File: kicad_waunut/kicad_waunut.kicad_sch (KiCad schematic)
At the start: 76 parts, among them J1 Conn_01x06_Pin, J2 Conn_01x02_Pin, U1 ATtiny861A-S

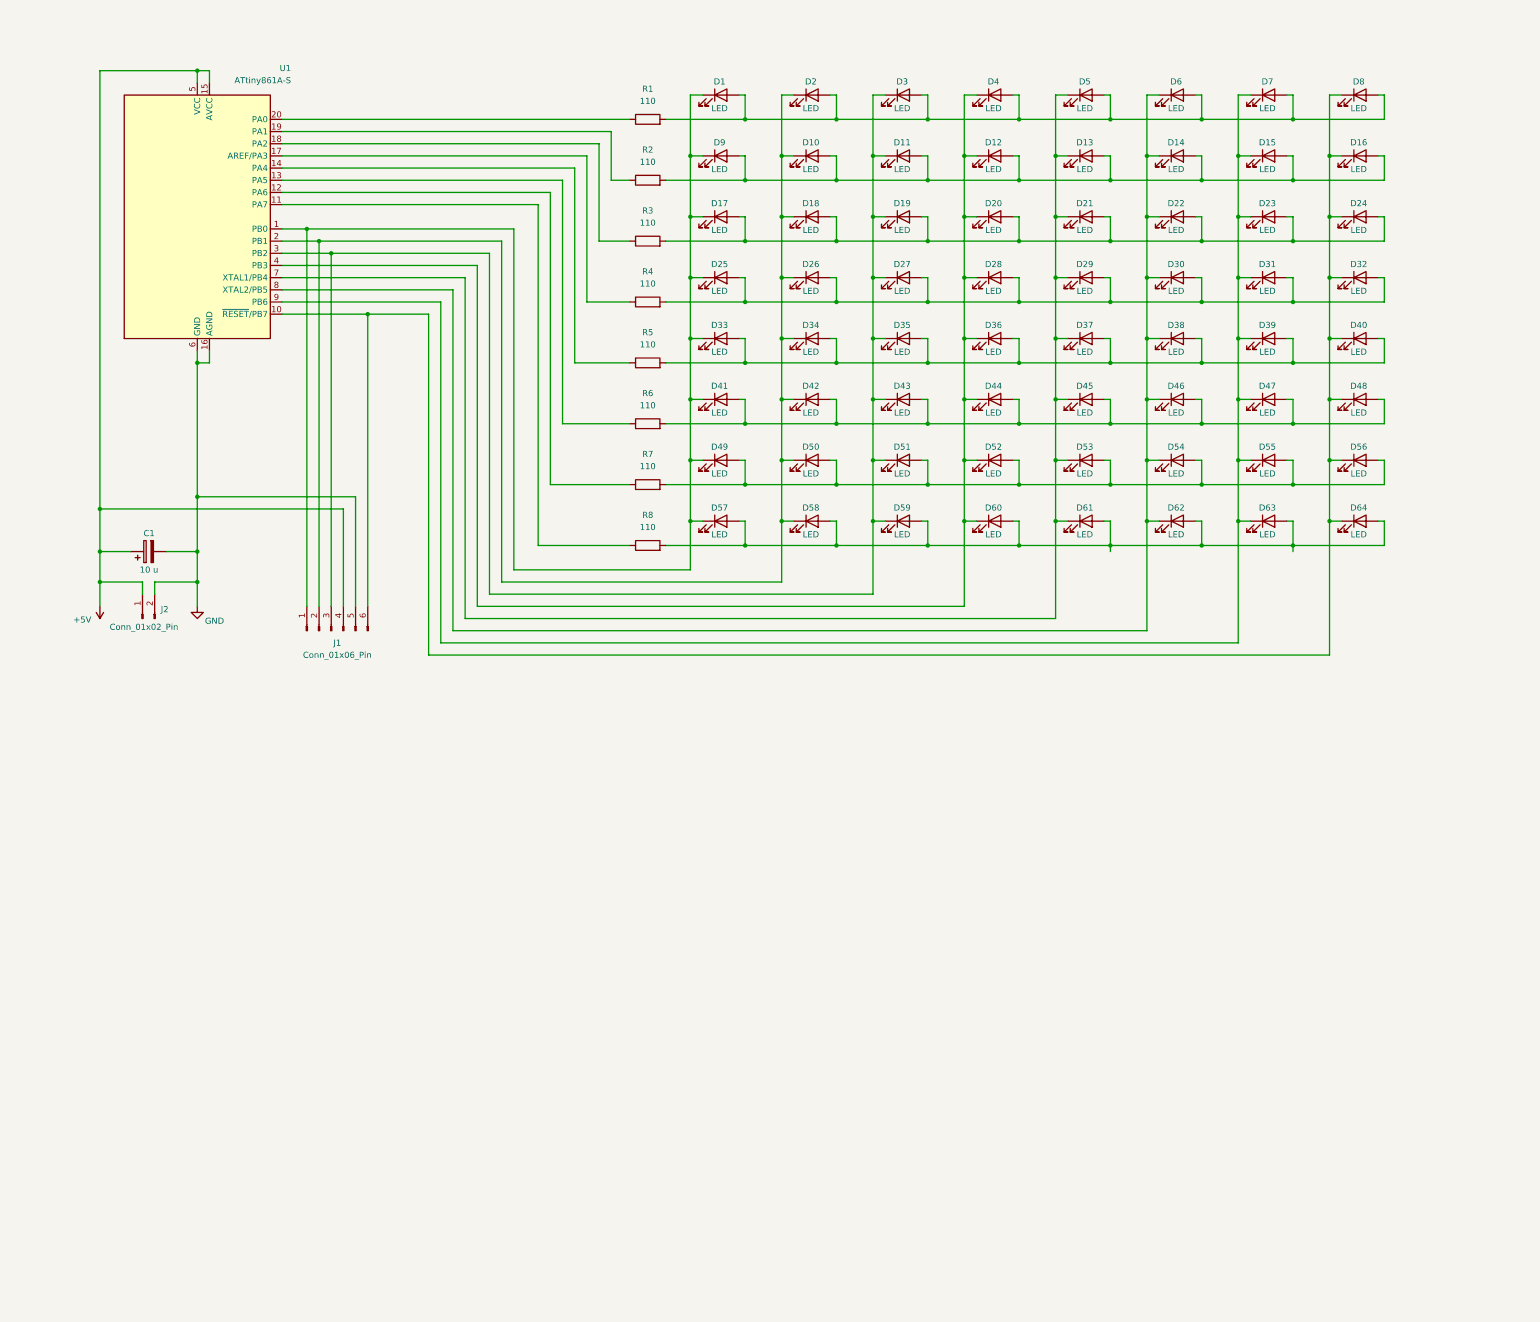
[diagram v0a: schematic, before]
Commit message: 2 lediä vilkkuu - vilkutus_2x.c
Jostain syystä kummallinen if statementti jossa 2 lediä palaa mutta eri
kirrkaudella.

Muutama ledi himmenee/kirkastuu. hmm...

Muuten jeba
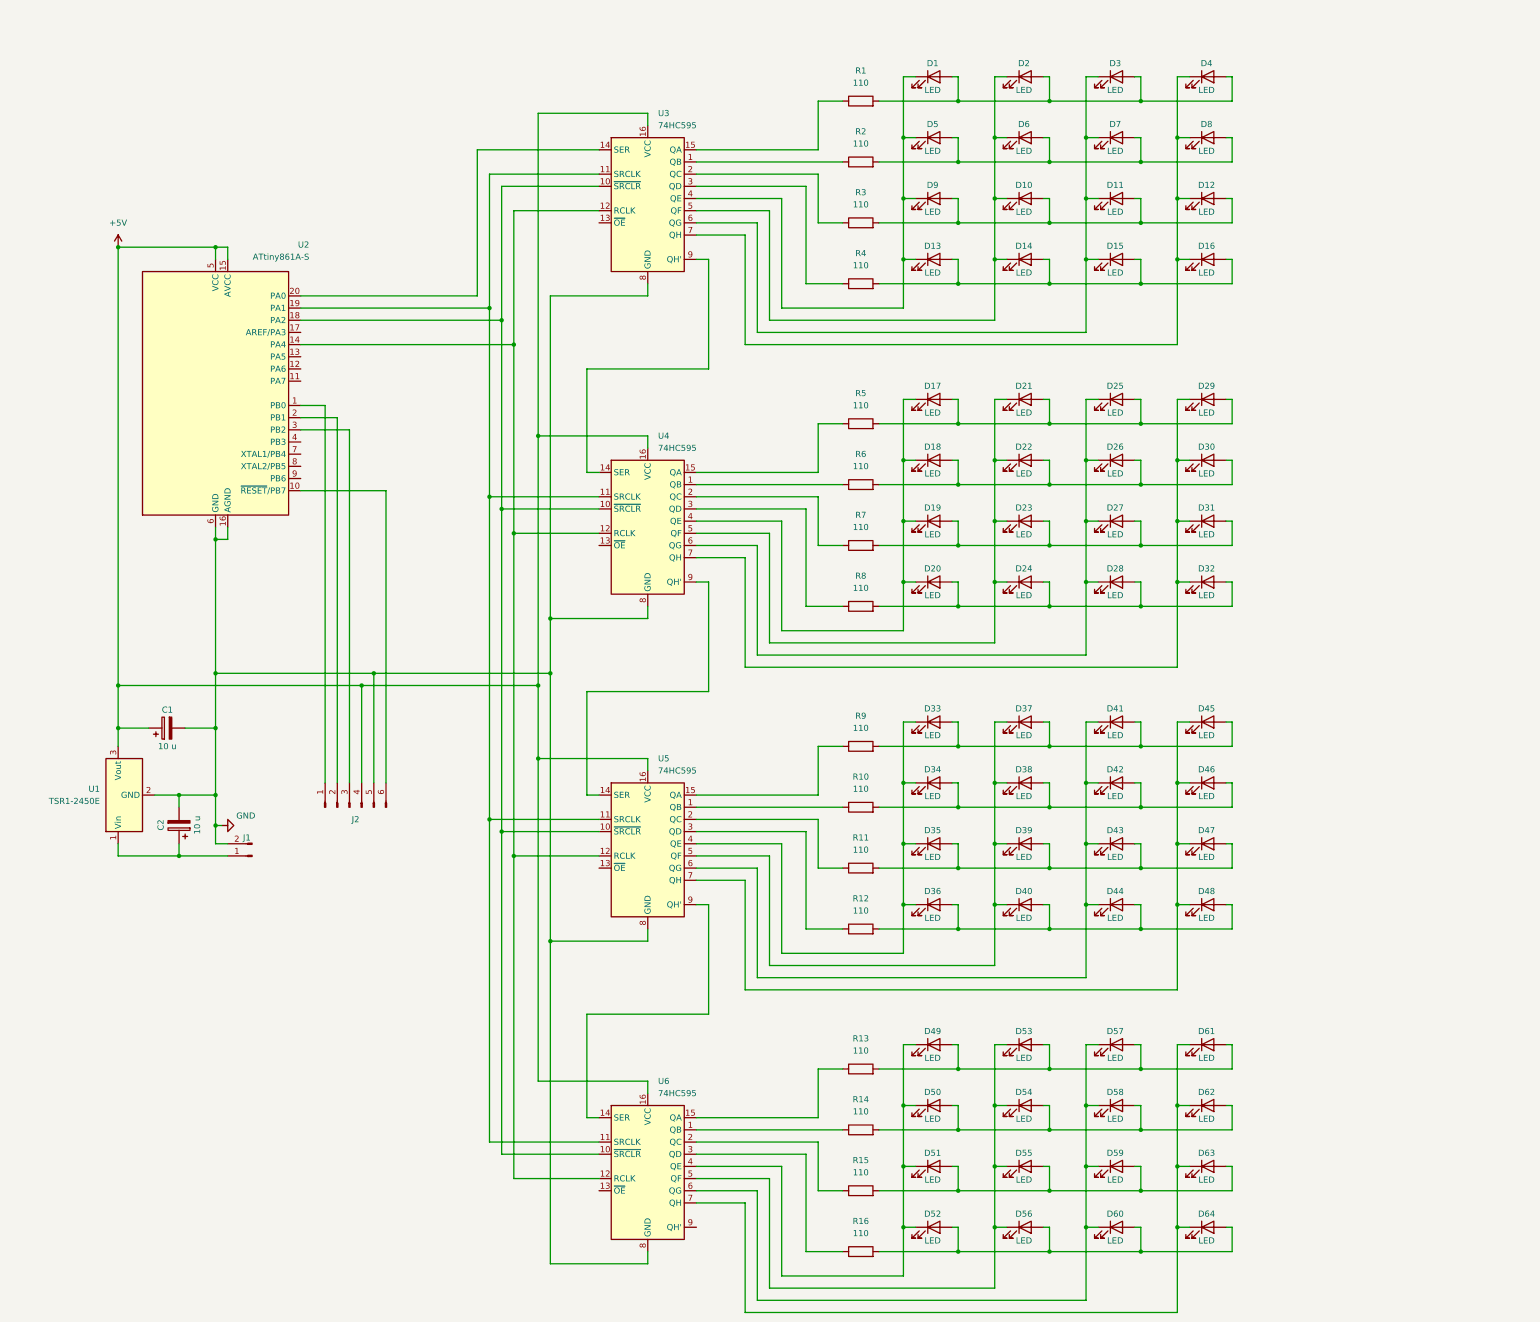
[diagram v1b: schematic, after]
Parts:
- added C2: 10 u, Capacitor_SMD:C_1210_3225Metric_Pad1.33x2.70mm_HandSolder, symbol Device:C_Polarized
- added R10, R11, R12, R13, R14, R15, R16, R9: 110, Resistor_SMD:R_1206_3216Metric_Pad1.30x1.75mm_HandSolder, symbol Device:R
- added U1: TSR1-2450E, Converter_DCDC:Converter_DCDC_TRACO_TSR-1_THT, symbol Regulator_Switching:TSR1-2450E
- added U3, U4, U5, U6: 74HC595, Package_SO:SOIC-16_3.9x9.9mm_P1.27mm, symbol 74xx:74HC595
- renumbered J2 to J1, J1 to J2, U1 to U2
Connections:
- net +5V: now also U1.3 (Vout), U3.16 (VCC), U4.16 (VCC), U5.16 (VCC), U6.16 (VCC); no longer J1.1 (Pin_1)
- net GND: now also C2.2, U1.2 (GND), U3.8 (GND), U4.8 (GND), U5.8 (GND), U6.8 (GND)
- net at D1.2 (A), D2.2 (A), D3.2 (A)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: no longer D5.2 (A), D6.2 (A), D7.2 (A), D8.2 (A)
- net at R4.1: now also U3.3 (QD); no longer U2.17 (AREF/PA3)
- net at R8.1: now also U4.3 (QD); no longer U2.11 (PA7)
- net at U2.18 (PA2): now also U3.10 (~{SRCLR}), U4.10 (~{SRCLR}), U5.10 (~{SRCLR}), U6.10 (~{SRCLR}); no longer R3.1
- net at U2.14 (PA4): now also U3.12 (RCLK), U4.12 (RCLK), U5.12 (RCLK), U6.12 (RCLK); no longer R5.1
- net at U2.20 (PA0): now also U3.14 (SER); no longer R1.1
- net at R6.1: now also U4.1 (QB); no longer U2.13 (PA5)
- net at R7.1: now also U4.2 (QC); no longer U2.12 (PA6)
- net at U2.19 (PA1): now also U3.11 (SRCLK), U4.11 (SRCLK), U5.11 (SRCLK), U6.11 (SRCLK); no longer R2.1
- new net: D45.1 (K), D46.1 (K), D47.1 (K), D48.1 (K), U5.7 (QH)
- new net: D36.2 (A), D40.2 (A), D44.2 (A), D48.2 (A), R12.2
- new net: D17.1 (K), D18.1 (K), D19.1 (K), D20.1 (K), U4.4 (QE)
- new net: D19.2 (A), D23.2 (A), D27.2 (A), D31.2 (A), R7.2
- new net: D21.1 (K), D22.1 (K), D23.1 (K), D24.1 (K), U4.5 (QF)
- new net: D17.2 (A), D21.2 (A), D25.2 (A), D29.2 (A), R5.2
- new net: D34.2 (A), D38.2 (A), D42.2 (A), D46.2 (A), R10.2
- new net: D20.2 (A), D24.2 (A), D28.2 (A), D32.2 (A), R8.2
- new net: D37.1 (K), D38.1 (K), D39.1 (K), D40.1 (K), U5.5 (QF)
- new net: D12.1 (K), D16.1 (K), D4.1 (K), D8.1 (K), U3.7 (QH)
- new net: D5.2 (A), D6.2 (A), D7.2 (A), D8.2 (A), R2.2
- new net: D41.1 (K), D42.1 (K), D43.1 (K), D44.1 (K), U5.6 (QG)
- new net: D53.1 (K), D54.1 (K), D55.1 (K), D56.1 (K), U6.5 (QF)
- new net: D52.2 (A), D56.2 (A), D60.2 (A), D64.2 (A), R16.2
- new net: D57.1 (K), D58.1 (K), D59.1 (K), D60.1 (K), U6.6 (QG)
- new net: D50.2 (A), D54.2 (A), D58.2 (A), D62.2 (A), R14.2
- new net: D29.1 (K), D30.1 (K), D31.1 (K), D32.1 (K), U4.7 (QH)
- new net: D35.2 (A), D39.2 (A), D43.2 (A), D47.2 (A), R11.2
- new net: D49.1 (K), D50.1 (K), D51.1 (K), D52.1 (K), U6.4 (QE)
- new net: D33.2 (A), D37.2 (A), D41.2 (A), D45.2 (A), R9.2
- new net: D51.2 (A), D55.2 (A), D59.2 (A), D63.2 (A), R15.2
- new net: R14.1, U6.1 (QB)
- new net: U5.9 (QH'), U6.14 (SER)
- new net: R13.1, U6.15 (QA)
- new net: R15.1, U6.2 (QC)
- new net: R16.1, U6.3 (QD)
- new net: D61.1 (K), D62.1 (K), D63.1 (K), D64.1 (K), U6.7 (QH)
- new net: R12.1, U5.3 (QD)
- new net: D13.2 (A), D14.2 (A), D15.2 (A), D16.2 (A), R4.2
- new net: C2.1, J1.1 (Pin_1), U1.1 (Vin)
- new net: D33.1 (K), D34.1 (K), D35.1 (K), D36.1 (K), U5.4 (QE)
- new net: D11.1 (K), D15.1 (K), D3.1 (K), D7.1 (K), U3.6 (QG)
- new net: D1.1 (K), D13.1 (K), D5.1 (K), D9.1 (K), U3.4 (QE)
- new net: D10.2 (A), D11.2 (A), D12.2 (A), D9.2 (A), R3.2
- new net: D25.1 (K), D26.1 (K), D27.1 (K), D28.1 (K), U4.6 (QG)
- new net: R3.1, U3.2 (QC)
- new net: R2.1, U3.1 (QB)
- new net: R1.1, U3.15 (QA)
- new net: D10.1 (K), D14.1 (K), D2.1 (K), D6.1 (K), U3.5 (QF)
- new net: U3.9 (QH'), U4.14 (SER)
- new net: D49.2 (A), D53.2 (A), D57.2 (A), D61.2 (A), R13.2
- new net: J2.1 (Pin_1), U2.1 (PB0)
- new net: J2.2 (Pin_2), U2.2 (PB1)
- new net: J2.3 (Pin_3), U2.3 (PB2)
- new net: J2.6 (Pin_6), U2.10 (~{RESET}/PB7)
- new net: D18.2 (A), D22.2 (A), D26.2 (A), D30.2 (A), R6.2
- new net: R5.1, U4.15 (QA)
- new net: U4.9 (QH'), U5.14 (SER)
- new net: R10.1, U5.1 (QB)
- new net: R9.1, U5.15 (QA)
- new net: R11.1, U5.2 (QC)
- now unconnected: U2.4 (PB3), U2.7 (XTAL1/PB4), U2.8 (XTAL2/PB5), U2.9 (PB6)
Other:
- moved on the sheet: C1, D1, J1, J2, R1, R2, R3, R4, U2

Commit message: Waunujen skemaa muutettu. README tiedostoja päivitetty.
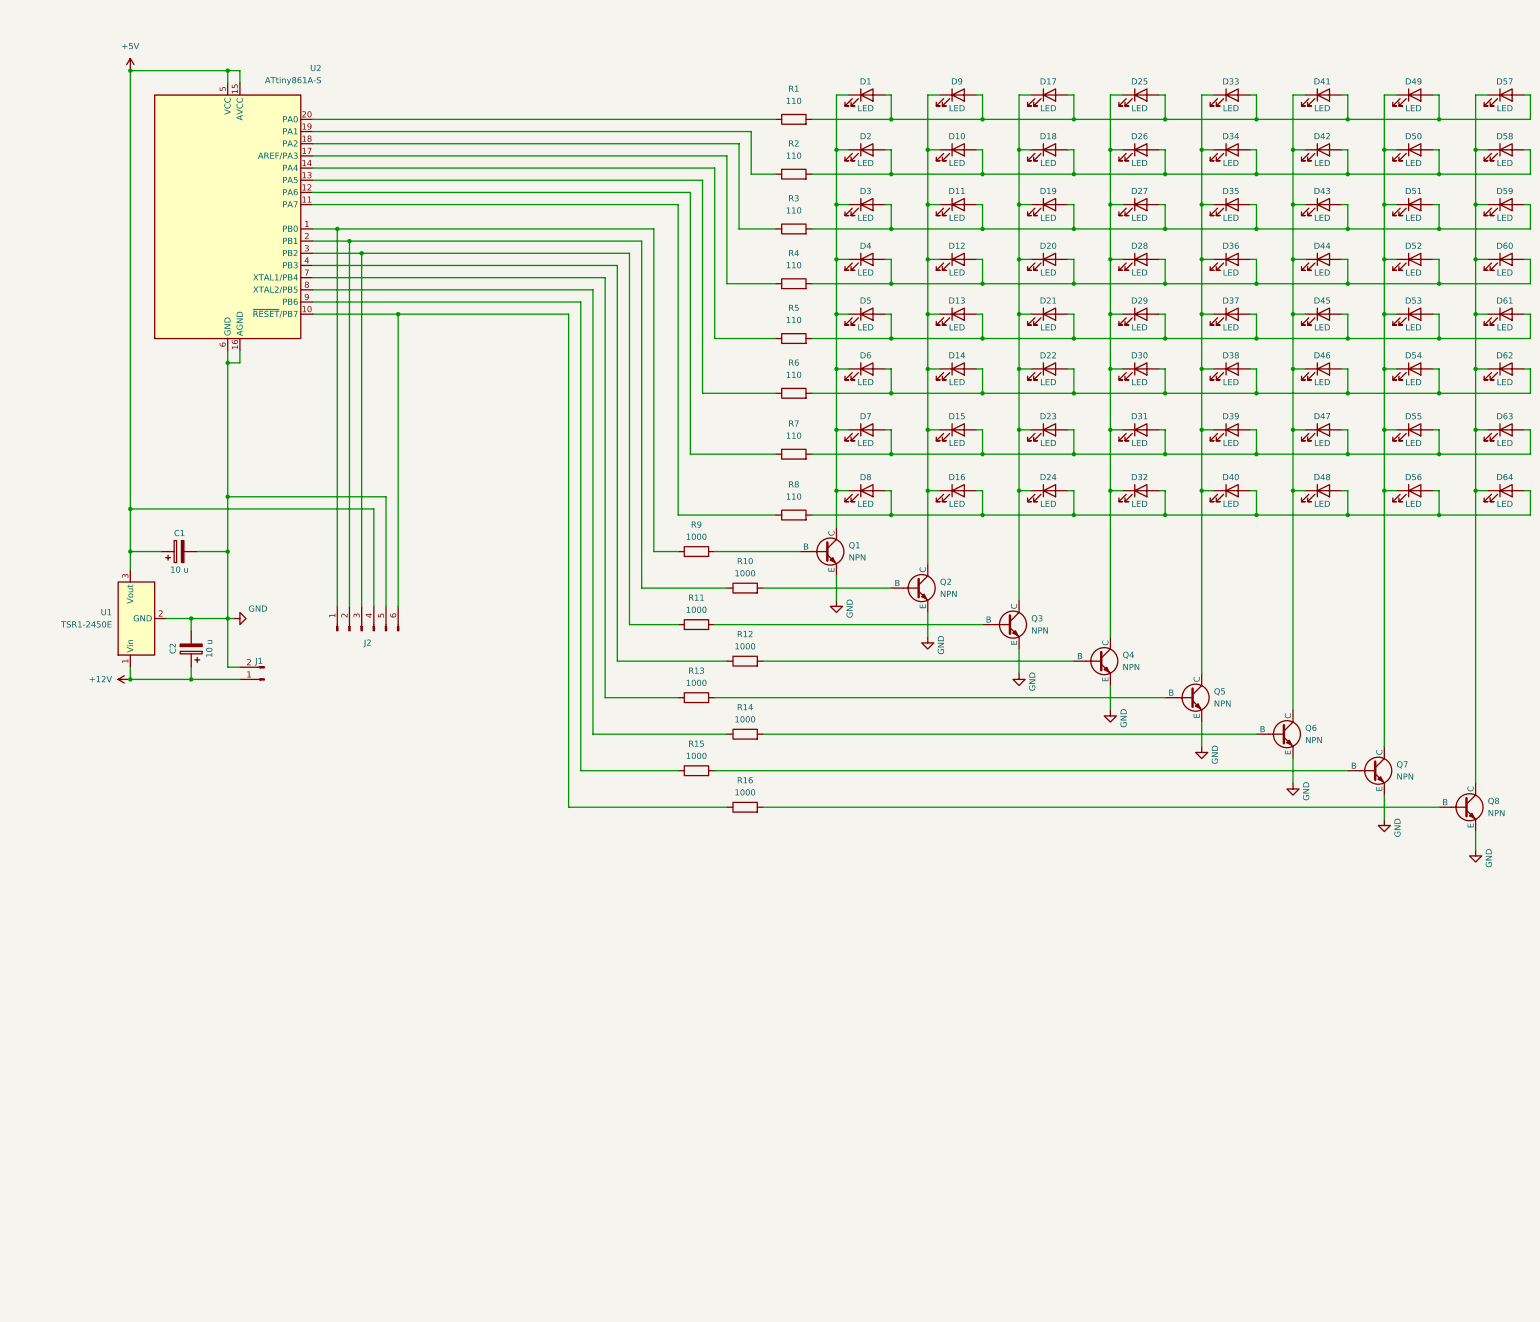
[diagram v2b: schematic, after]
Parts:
- removed U3, U4, U5, U6: 74HC595, Package_SO:SOIC-16_3.9x9.9mm_P1.27mm, symbol 74xx:74HC595
- added Q1, Q2, Q3, Q4, Q5, Q6, Q7, Q8: NPN, Package_TO_SOT_SMD:SOT-23, symbol Simulation_SPICE:NPN
- R10, R11, R12, R13, R14, R15, R16, R9: value 110 -> 1000
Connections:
- net GND: now also Q1.3 (E), Q2.3 (E), Q3.3 (E), Q4.3 (E), Q5.3 (E), Q6.3 (E), Q7.3 (E), Q8.3 (E)
- net at D45.1 (K), D46.1 (K), D47.1 (K)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: now also D41.1 (K), D42.1 (K), D43.1 (K), D44.1 (K), Q6.1 (C)
- net at D17.1 (K), D18.1 (K), D19.1 (K)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: now also D21.1 (K), D22.1 (K), D23.1 (K), D24.1 (K), Q3.1 (C)
- net at D23.2 (A), D31.2 (A), R7.2: now also D15.2 (A), D39.2 (A), D47.2 (A), D55.2 (A), D63.2 (A), D7.2 (A); no longer D19.2 (A), D27.2 (A)
- net at D21.2 (A), D29.2 (A), R5.2: now also D13.2 (A), D37.2 (A), D45.2 (A), D5.2 (A), D53.2 (A), D61.2 (A); no longer D17.2 (A), D25.2 (A)
- net at D24.2 (A), D32.2 (A), R8.2: now also D16.2 (A), D40.2 (A), D48.2 (A), D56.2 (A), D64.2 (A), D8.2 (A); no longer D20.2 (A), D28.2 (A)
- net at D37.1 (K), D38.1 (K), D39.1 (K)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: now also D33.1 (K), D34.1 (K), D35.1 (K), D36.1 (K), Q5.1 (C)
- net at D4.1 (K), D8.1 (K): now also D1.1 (K), D2.1 (K), D3.1 (K), D5.1 (K), D6.1 (K), D7.1 (K), Q1.1 (C); no longer D12.1 (K), D16.1 (K)
- net at D53.1 (K), D54.1 (K), D55.1 (K)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: now also D49.1 (K), D50.1 (K), D51.1 (K), D52.1 (K), Q7.1 (C)
- net at D57.1 (K), D58.1 (K), D59.1 (K)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: now also D61.1 (K), D62.1 (K), D63.1 (K), D64.1 (K), Q8.1 (C)
- net at D29.1 (K), D30.1 (K), D31.1 (K)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: now also D25.1 (K), D26.1 (K), D27.1 (K), D28.1 (K), Q4.1 (C)
- net at R14.1: now also U2.8 (XTAL2/PB5)
- net at U2.18 (PA2): now also R3.1
- net at U2.19 (PA1): now also R2.1
- net at U2.14 (PA4): now also R5.1
- net at R13.1: now also U2.7 (XTAL1/PB4)
- net at R15.1: now also U2.9 (PB6)
- net at R16.1: now also J2.6 (Pin_6), U2.10 (~{RESET}/PB7)
- net at R12.1: now also U2.4 (PB3)
- net at R4.1: now also U2.17 (AREF/PA3)
- net +12V: now reaches C2.1, J1.1 (Pin_1), U1.1 (Vin)
- net at D11.1 (K), D15.1 (K): now also D10.1 (K), D12.1 (K), D13.1 (K), D14.1 (K), D16.1 (K), D9.1 (K), Q2.1 (C); no longer D3.1 (K), D7.1 (K)
- net at R8.1: now also U2.11 (PA7)
- net at U2.20 (PA0): now also R1.1
- net at J2.1 (Pin_1), U2.1 (PB0): now also R9.1
- net at J2.2 (Pin_2), U2.2 (PB1): now also R10.1
- net at J2.3 (Pin_3), U2.3 (PB2): now also R11.1
- net at D22.2 (A), D30.2 (A), R6.2: now also D14.2 (A), D38.2 (A), D46.2 (A), D54.2 (A), D6.2 (A), D62.2 (A); no longer D18.2 (A), D26.2 (A)
- net at R6.1: now also U2.13 (PA5)
- net at R7.1: now also U2.12 (PA6)
- new net: D12.2 (A), D20.2 (A), D28.2 (A), D36.2 (A), D4.2 (A), D44.2 (A), D52.2 (A), D60.2 (A), R4.2
- new net: Q1.2 (B), R9.2
- new net: D1.2 (A), D17.2 (A), D25.2 (A), D33.2 (A), D41.2 (A), D49.2 (A), D57.2 (A), D9.2 (A), R1.2
- new net: Q3.2 (B), R11.2
- new net: D11.2 (A), D19.2 (A), D27.2 (A), D3.2 (A), D35.2 (A), D43.2 (A), D51.2 (A), D59.2 (A), R3.2
- new net: Q4.2 (B), R12.2
- new net: Q2.2 (B), R10.2
- new net: Q5.2 (B), R13.2
- new net: Q8.2 (B), R16.2
- new net: Q6.2 (B), R14.2
- new net: D10.2 (A), D18.2 (A), D2.2 (A), D26.2 (A), D34.2 (A), D42.2 (A), D50.2 (A), D58.2 (A), R2.2
- new net: Q7.2 (B), R15.2
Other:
- moved on the sheet: C1, C2, D1, J1, J2, R1, R2, R3, R4, U1, U2
